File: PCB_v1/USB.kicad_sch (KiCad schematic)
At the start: 1 part, among them J1 1051640001

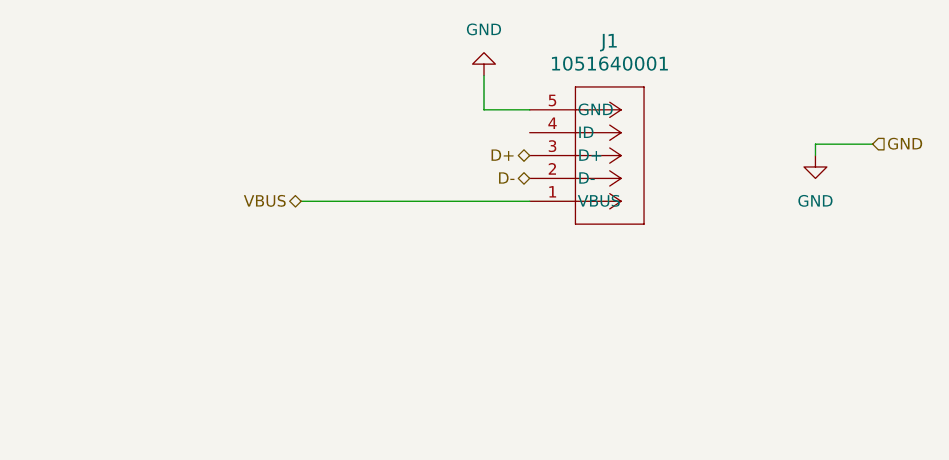
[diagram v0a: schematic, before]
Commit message: changed debouncing order, switches to jst, and array resistors
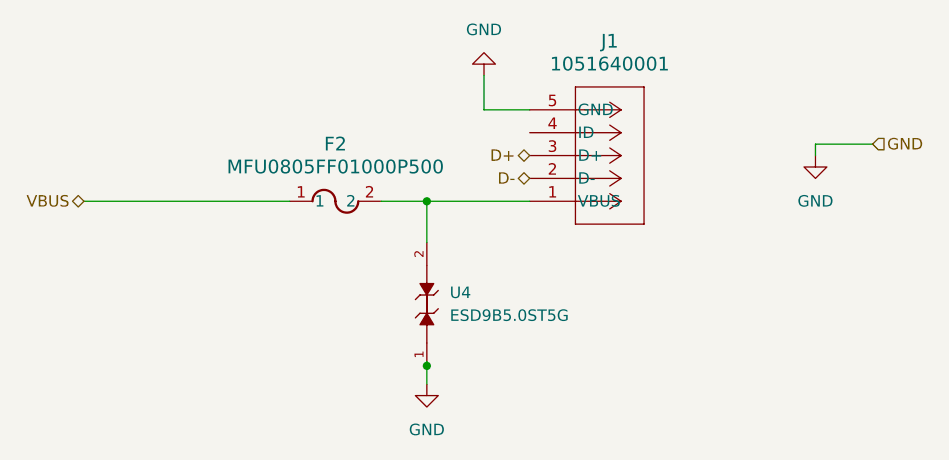
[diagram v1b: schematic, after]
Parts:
- added F2: MFU0805FF01000P500, FUS_VISHAY_MFU0805_VIS, symbol GT_LIbrary:MFU0805FF01000P500
- added U4: ESD9B5.0ST5G, ESD9B5.0ST5G:SODFL1006X40N, symbol GT_LIbrary:ESD9B5.0ST5G
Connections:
- net GND: now also U4.1
- net VBUS: now also F2.1; no longer J1.1 (VBUS)
- new net: F2.2, J1.1 (VBUS), U4.2

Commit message: Update before adding AGND for the power delivery
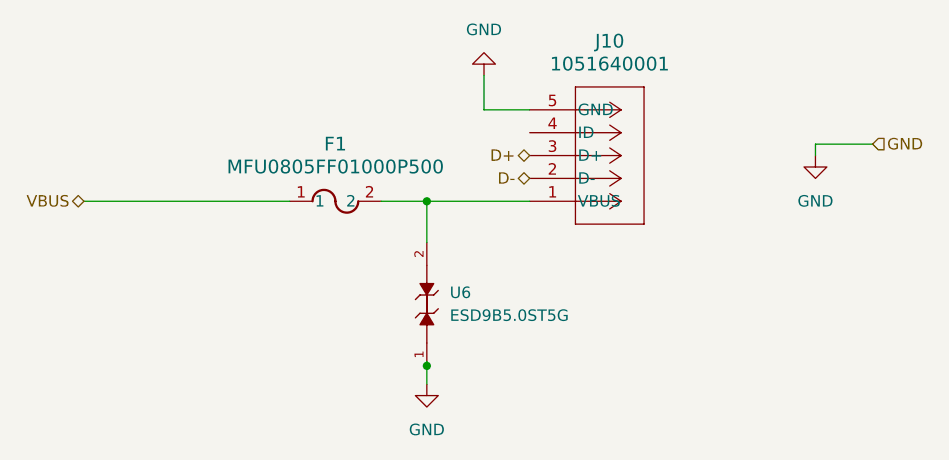
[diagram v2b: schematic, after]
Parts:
- renumbered F2 to F1, J1 to J10, U4 to U6
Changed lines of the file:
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@@
 		(dnp no)
 		(fields_autoplaced yes)
-		(property "Reference" "U4"
+		(property "Reference" "U6"
 			(at 156.21 92.7099 90)
 			(effects
@@
 			(project ""
 				(path "/353cef6a-fb6e-40d9-89f8-eb54b7aa5118/0c3109f9-2cf7-4151-a3d7-47dc50d219a6"
-					(reference "U4")
+					(reference "U6")
 					(unit 1)
 				)
@@
 		(dnp no)
 		(fields_autoplaced yes)
-		(property "Reference" "F2"
+		(property "Reference" "F1"
 			(at 143.51 76.2 0)
 			(effects
@@
 			(project "tuner time"
 				(path "/353cef6a-fb6e-40d9-89f8-eb54b7aa5118/0c3109f9-2cf7-4151-a3d7-47dc50d219a6"
-					(reference "F2")
+					(reference "F1")
 					(unit 1)
 				)
@@
 		(dnp no)
 		(fields_autoplaced yes)
-		(property "Reference" "J1"
+		(property "Reference" "J10"
 			(at 173.99 64.77 0)
 			(effects
@@
 			(project "tuner time"
 				(path "/353cef6a-fb6e-40d9-89f8-eb54b7aa5118/0c3109f9-2cf7-4151-a3d7-47dc50d219a6"
-					(reference "J1")
+					(reference "J10")
 					(unit 1)
 				)
@@
 		(dnp no)
 		(fields_autoplaced yes)
-		(property "Reference" "#PWR014"
+		(property "Reference" "#PWR0101"
 			(at 160.02 62.23 0)
 			(effects
@@
 			(project "tuner time"
 				(path "/353cef6a-fb6e-40d9-89f8-eb54b7aa5118/0c3109f9-2cf7-4151-a3d7-47dc50d219a6"
-					(reference "#PWR014")
+					(reference "#PWR0101")
 					(unit 1)
 				)
@@
 		(dnp no)
 		(fields_autoplaced yes)
-		(property "Reference" "#PWR016"
+		(property "Reference" "#PWR0100"
 			(at 153.67 109.22 0)
 			(effects
@@
 			(project "tuner time"
 				(path "/353cef6a-fb6e-40d9-89f8-eb54b7aa5118/0c3109f9-2cf7-4151-a3d7-47dc50d219a6"
-					(reference "#PWR016")
+					(reference "#PWR0100")
 					(unit 1)
 				)
@@
 		(dnp no)
 		(fields_autoplaced yes)
-		(property "Reference" "#PWR0106"
+		(property "Reference" "#PWR0102"
 			(at 196.85 83.82 0)
 			(effects
@@
 			(project "tuner time"
 				(path "/353cef6a-fb6e-40d9-89f8-eb54b7aa5118/0c3109f9-2cf7-4151-a3d7-47dc50d219a6"
-					(reference "#PWR0106")
+					(reference "#PWR0102")
 					(unit 1)
 				)

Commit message: Initial placement draft
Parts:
- U6: footprint ESD9B5.0ST5G:SODFL1006X40N -> Parts_Library:SODFL1006X40N
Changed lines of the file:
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@@
 			)
 		)
-		(property "Footprint" "ESD9B5.0ST5G:SODFL1006X40N"
+		(property "Footprint" "Parts_Library:SODFL1006X40N"
 			(at 153.67 93.98 0)
 			(effects
@@
 		)
 		(property "SnapEDA_Link" ""
+			(at 153.67 93.98 0)
+			(effects
+				(font
+					(size 1.27 1.27)
+				)
+				(hide yes)
+			)
+		)
+		(property "MFP" ""
 			(at 153.67 93.98 0)
 			(effects
@@
 		)
 		(property "SnapEDA_Link" ""
+			(at 138.43 82.55 0)
+			(effects
+				(font
+					(size 1.27 1.27)
+				)
+				(hide yes)
+			)
+		)
+		(property "MFP" ""
 			(at 138.43 82.55 0)
 			(effects
@@
 			)
 		)
+		(property "MFP" ""
+			(at 165.1 82.55 0)
+			(effects
+				(font
+					(size 1.27 1.27)
+				)
+				(hide yes)
+			)
+		)
 		(pin "1"
 		)
@@
 		(dnp no)
 		(fields_autoplaced yes)
-		(property "Reference" "#PWR0101"
+		(property "Reference" "#PWR0109"
 			(at 160.02 62.23 0)
 			(effects
@@
 			(project "tuner time"
 				(path "/353cef6a-fb6e-40d9-89f8-eb54b7aa5118/0c3109f9-2cf7-4151-a3d7-47dc50d219a6"
-					(reference "#PWR0101")
+					(reference "#PWR0109")
 					(unit 1)
 				)
@@
 		(dnp no)
 		(fields_autoplaced yes)
-		(property "Reference" "#PWR0100"
+		(property "Reference" "#PWR0108"
 			(at 153.67 109.22 0)
 			(effects
@@
 			(project "tuner time"
 				(path "/353cef6a-fb6e-40d9-89f8-eb54b7aa5118/0c3109f9-2cf7-4151-a3d7-47dc50d219a6"
-					(reference "#PWR0100")
+					(reference "#PWR0108")
 					(unit 1)
 				)
@@
 		(dnp no)
 		(fields_autoplaced yes)
-		(property "Reference" "#PWR0102"
+		(property "Reference" "#PWR0110"
 			(at 196.85 83.82 0)
 			(effects
@@
 			(project "tuner time"
 				(path "/353cef6a-fb6e-40d9-89f8-eb54b7aa5118/0c3109f9-2cf7-4151-a3d7-47dc50d219a6"
-					(reference "#PWR0102")
+					(reference "#PWR0110")
 					(unit 1)
 				)

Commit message: pushing BOM
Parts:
- F2: renamed from F1; MFP (none) -> MFU0805FF01000P500
- J10: MFP (none) -> 1051640001
- U7: renamed from U6; MFP (none) -> ESD9B5.0ST5G
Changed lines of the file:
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@@
 		(dnp no)
 		(fields_autoplaced yes)
-		(property "Reference" "U6"
+		(property "Reference" "U7"
 			(at 156.21 92.7099 90)
 			(effects
@@
 			)
 		)
-		(property "MFP" ""
+		(property "MFP" "ESD9B5.0ST5G"
 			(at 153.67 93.98 0)
 			(effects
@@
 			(project ""
 				(path "/353cef6a-fb6e-40d9-89f8-eb54b7aa5118/0c3109f9-2cf7-4151-a3d7-47dc50d219a6"
-					(reference "U6")
+					(reference "U7")
 					(unit 1)
 				)
@@
 		(dnp no)
 		(fields_autoplaced yes)
-		(property "Reference" "F1"
+		(property "Reference" "F2"
 			(at 143.51 76.2 0)
 			(effects
@@
 			)
 		)
-		(property "Datasheet" "MFU0805FF01000P500"
+		(property "Datasheet" ""
 			(at 138.43 82.55 0)
 			(effects
@@
 			)
 		)
-		(property "MFP" ""
+		(property "MFP" "MFU0805FF01000P500"
 			(at 138.43 82.55 0)
 			(effects
@@
 			(project "tuner time"
 				(path "/353cef6a-fb6e-40d9-89f8-eb54b7aa5118/0c3109f9-2cf7-4151-a3d7-47dc50d219a6"
-					(reference "F1")
+					(reference "F2")
 					(unit 1)
 				)
@@
 			)
 		)
-		(property "MFP" ""
+		(property "MFP" "1051640001"
 			(at 165.1 82.55 0)
 			(effects
@@
 		(dnp no)
 		(fields_autoplaced yes)
-		(property "Reference" "#PWR0113"
+		(property "Reference" "#PWR0127"
 			(at 160.02 62.23 0)
 			(effects
@@
 			(project "tuner time"
 				(path "/353cef6a-fb6e-40d9-89f8-eb54b7aa5118/0c3109f9-2cf7-4151-a3d7-47dc50d219a6"
-					(reference "#PWR0113")
+					(reference "#PWR0127")
 					(unit 1)
 				)
@@
 		(dnp no)
 		(fields_autoplaced yes)
-		(property "Reference" "#PWR0112"
+		(property "Reference" "#PWR0126"
 			(at 153.67 109.22 0)
 			(effects
@@
 			(project "tuner time"
 				(path "/353cef6a-fb6e-40d9-89f8-eb54b7aa5118/0c3109f9-2cf7-4151-a3d7-47dc50d219a6"
-					(reference "#PWR0112")
+					(reference "#PWR0126")
 					(unit 1)
 				)
@@
 		(dnp no)
 		(fields_autoplaced yes)
-		(property "Reference" "#PWR0114"
+		(property "Reference" "#PWR0128"
 			(at 196.85 83.82 0)
 			(effects
@@
 			(project "tuner time"
 				(path "/353cef6a-fb6e-40d9-89f8-eb54b7aa5118/0c3109f9-2cf7-4151-a3d7-47dc50d219a6"
-					(reference "#PWR0114")
+					(reference "#PWR0128")
 					(unit 1)
 				)

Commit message: adding the crystal
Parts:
- J10: symbol 2025-02-12_14-59-21:1051640001 -> GT_LIbrary:1051640001
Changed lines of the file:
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@@
 	)
 	(symbol
-		(lib_id "2025-02-12_14-59-21:1051640001")
+		(lib_id "GT_LIbrary:1051640001")
 		(at 165.1 82.55 0)
 		(mirror x)
@@
 	)
 	(symbol
-		(lib_id "power:GND")
+		(lib_id "GT_LIbrary:GND")
 		(at 160.02 68.58 0)
 		(mirror x)
@@
 	)
 	(symbol
-		(lib_id "power:GND")
+		(lib_id "GT_LIbrary:GND")
 		(at 153.67 102.87 0)
 		(unit 1)
@@
 	)
 	(symbol
-		(lib_id "power:GND")
+		(lib_id "GT_LIbrary:GND")
 		(at 196.85 77.47 0)
 		(unit 1)

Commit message: before oscilator
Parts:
- U7: footprint Parts_Library:SODFL1006X40N -> ESD9B5.0ST5G:SODFL1006X40N
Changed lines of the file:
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@@
 			)
 		)
-		(property "Footprint" "Parts_Library:SODFL1006X40N"
+		(property "Footprint" "ESD9B5.0ST5G:SODFL1006X40N"
 			(at 153.67 93.98 0)
 			(effects
@@
 			)
 		)
-		(property "Datasheet" ""
+		(property "Datasheet" "MFU0805FF01000P500"
 			(at 138.43 82.55 0)
 			(effects
